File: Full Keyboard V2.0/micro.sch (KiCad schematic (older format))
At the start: 10 parts, among them J1 Conn_01x26, U1 AT24C02, U3 CD74HC4067SM

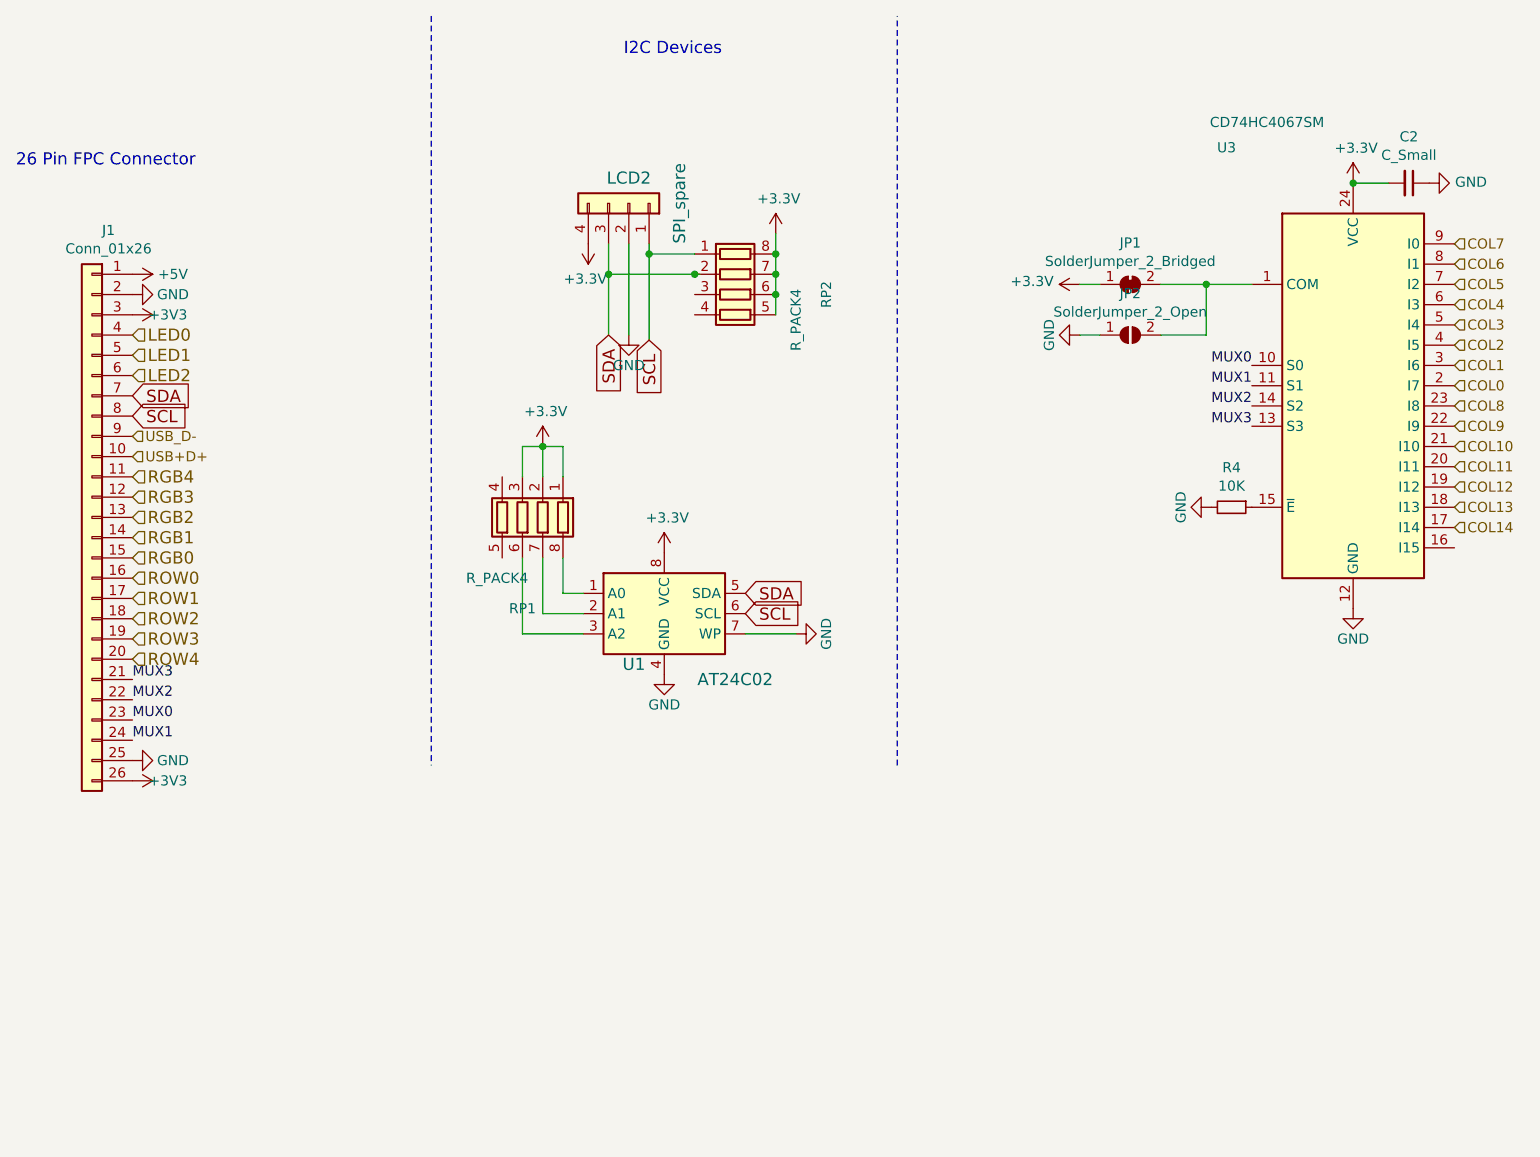
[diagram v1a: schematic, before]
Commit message: Added solder jumpers to allow for daisy chaining RGB rows
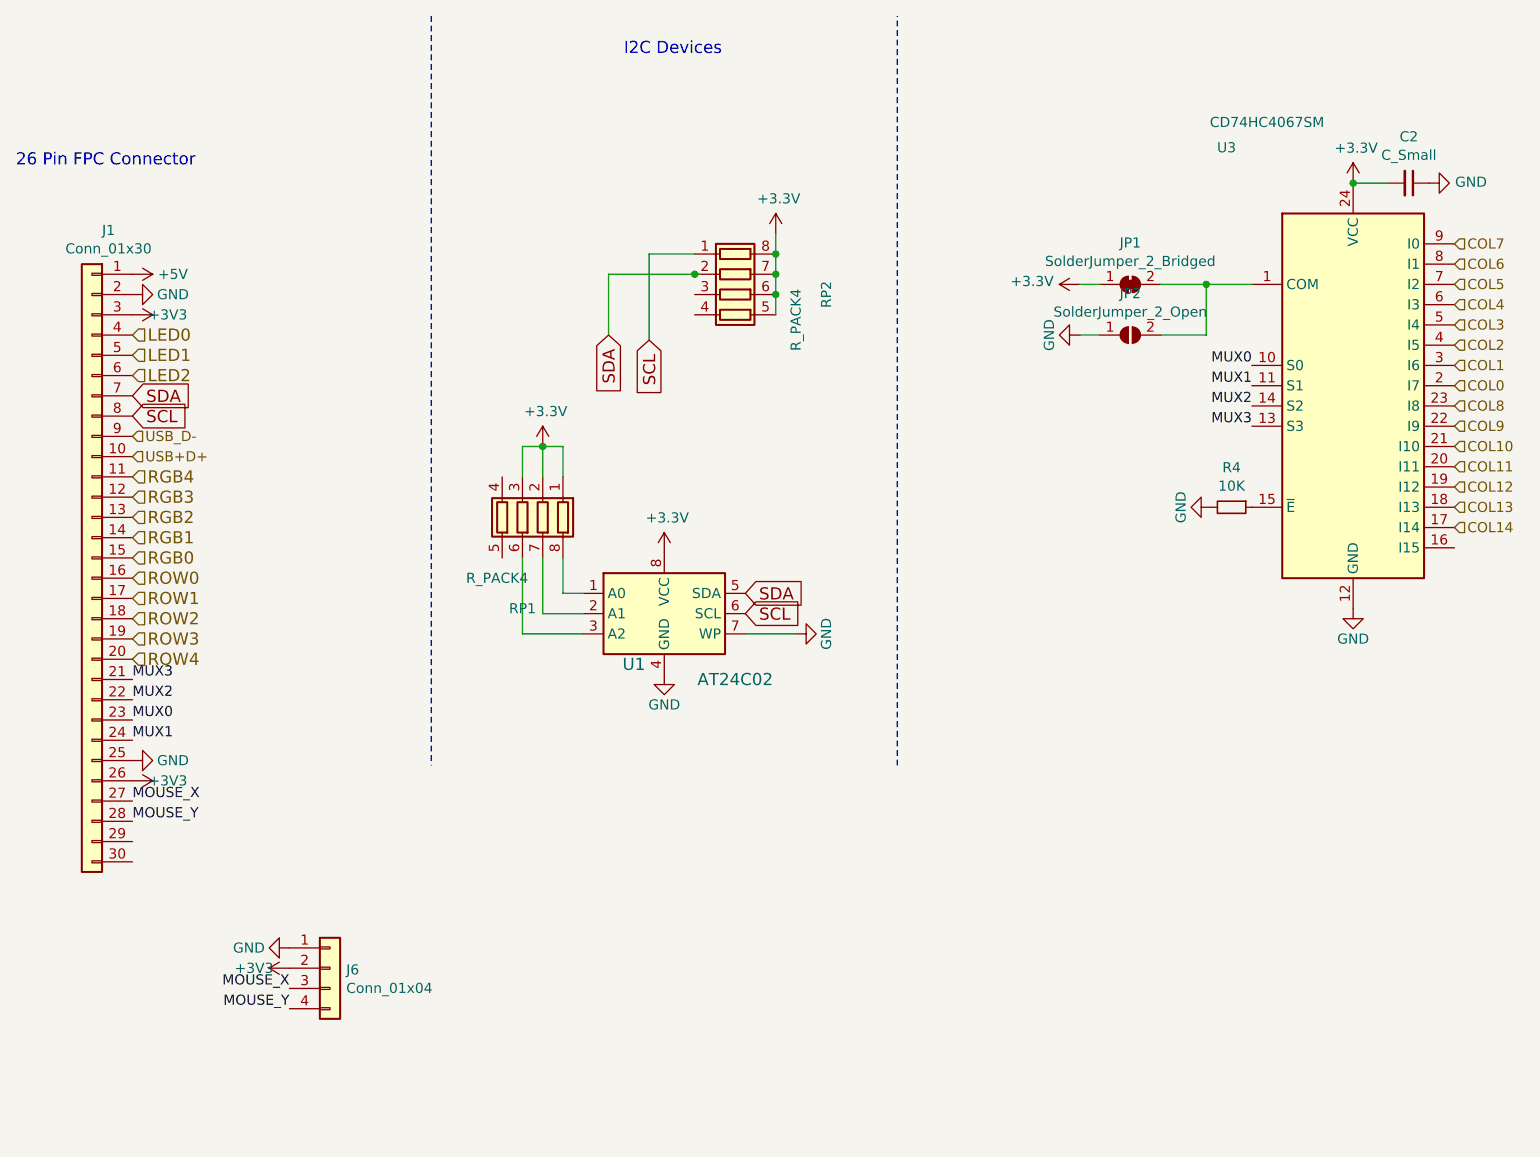
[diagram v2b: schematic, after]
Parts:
- removed J1: Conn_01x26, Connector_FFC-FPC:Hirose_FH12-26S-0.5SH_1x26-1MP_P0.50mm_Horizontal, symbol Connector_Generic:Conn_01x26
- removed LCD2: SPI_spare, Connector_PinHeader_2.54mm:PinHeader_1x04_P2.54mm_Vertical_SMD_Pin1Left, symbol Connector_Generic:Conn_01x04
- added J1: Conn_01x30, Connector_FFC-FPC:Hirose_FH12-30S-0.5SH_1x30-1MP_P0.50mm_Horizontal, symbol Connector_Generic:Conn_01x30
- added J6: Conn_01x04, Connector_JST:JST_PH_S4B-PH-SM4-TB_1x04-1MP_P2.00mm_Horizontal, symbol Connector_Generic:Conn_01x04
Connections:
- net labels added: MOUSE_X, MOUSE_Y
- wire segments 31 -> 28
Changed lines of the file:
@@
 $Descr A4 11693 8268
 encoding utf-8
-Sheet 3 4
+Sheet 2 4
 Title ""
 Date ""
@@
 	0    1    1    0
 $EndComp
-$Comp
-L Connector_Generic:Conn_01x04 LCD2
-U 1 1 59BADB3C
-P 5575 2775
-F 0 "LCD2" V 5700 2775 60  0000 C CNN
-F 1 "SPI_spare" H 5575 3025 60  0000 C CNN
-F 2 "Connector_PinHeader_2.54mm:PinHeader_1x04_P2.54mm_Vertical_SMD_Pin1Left" H 5575 2775 60  0001 C CNN
-F 3 "" H 5575 2775 60  0000 C CNN
-	1    5575 2775
-	0    1    -1   0
-$EndComp
 Text GLabel 5475 3425 3    60   Input ~ 0
 SDA
 Text GLabel 5675 3450 3    60   Input ~ 0
 SCL
-$Comp
-L power:GND #PWR0175
-U 1 1 59BADB44
-P 5575 3425
-F 0 "#PWR0175" H 5575 3175 50  0001 C CNN
-F 1 "GND" H 5575 3275 50  0000 C CNN
-F 2 "" H 5575 3425 50  0000 C CNN
-F 3 "" H 5575 3425 50  0000 C CNN
-	1    5575 3425
-	1    0    0    -1
-$EndComp
 Wire Wire Line
 	6400 4900 6150 4900
@@
 Wire Wire Line
 	5050 4900 5350 4900
-Wire Wire Line
-	5475 2975 5475 3125
 Wire Notes Line
 	6900 5550 6900 1850
@@
 Wire Wire Line
 	5900 3025 5675 3025
-Wire Wire Line
-	5675 2975 5675 3025
-Connection ~ 5675 3025
 Wire Wire Line
 	5675 3025 5675 3450
@@
 ROW0
 $Comp
-L Connector_Generic:Conn_01x26 J1
-U 1 1 5EAC1DE2
-P 2925 4325
-F 0 "J1" H 2843 5742 50  0000 C CNN
-F 1 "Conn_01x26" H 2843 5651 50  0000 C CNN
-F 2 "Connector_FFC-FPC:Hirose_FH12-26S-0.5SH_1x26-1MP_P0.50mm_Horizontal" H 2925 4325 50  0001 C CNN
-F 3 "~" H 2925 4325 50  0001 C CNN
-	1    2925 4325
-	-1   0    0    -1
-$EndComp
-$Comp
 L FullKeyboardV1-cache:+3.3V #PWR0168
 U 1 1 616DAE3A
@@
 $EndComp
 $Comp
-L FullKeyboardV1-cache:+3.3V #PWR0174
-U 1 1 616E0DE4
-P 5375 2975
-F 0 "#PWR0174" H 5375 2825 50  0001 C CNN
-F 1 "+3.3V" H 5390 3148 50  0000 C CNN
-F 2 "" H 5375 2975 50  0001 C CNN
-F 3 "" H 5375 2975 50  0001 C CNN
-	1    5375 2975
-	-1   0    0    1
-$EndComp
-$Comp
 L power:+3V3 #PWR0176
 U 1 1 616E35FA
@@
 $EndComp
 Wire Wire Line
-	5575 2975 5575 3425
-Wire Wire Line
 	5925 3125 5900 3125
 Connection ~ 5900 3125
@@
 Wire Wire Line
 	5475 3425 5475 3125
-Connection ~ 5475 3125
 $Comp
 L Device:R_Pack04 RP1
@@
 	0    1    1    0
 $EndComp
+$Comp
+L Connector_Generic:Conn_01x30 J1
+U 1 1 5E9DC884
+P 2925 4525
+F 0 "J1" H 2843 6142 50  0000 C CNN
+F 1 "Conn_01x30" H 2843 6051 50  0000 C CNN
+F 2 "Connector_FFC-FPC:Hirose_FH12-30S-0.5SH_1x30-1MP_P0.50mm_Horizontal" H 2925 4525 50  0001 C CNN
+F 3 "~" H 2925 4525 50  0001 C CNN
+	1    2925 4525
+	-1   0    0    -1
+$EndComp
+$Comp
+L Connector_Generic:Conn_01x04 J6
+U 1 1 5E9E6B8A
+P 4100 6550
+F 0 "J6" H 4180 6542 50  0000 L CNN
+F 1 "Conn_01x04" H 4180 6451 50  0000 L CNN
+F 2 "Connector_JST:JST_PH_S4B-PH-SM4-TB_1x04-1MP_P2.00mm_Horizontal" H 4100 6550 50  0001 C CNN
+F 3 "~" H 4100 6550 50  0001 C CNN
+	1    4100 6550
+	1    0    0    -1
+$EndComp
+Text Label 3900 6650 2    50   ~ 0
+MOUSE_X
+Text Label 3900 6750 2    50   ~ 0
+MOUSE_Y
+$Comp
+L power:+3V3 #PWR0166
+U 1 1 5E9E9956
+P 3900 6550
+F 0 "#PWR0166" H 3900 6400 50  0001 C CNN
+F 1 "+3V3" V 3900 6725 50  0000 C CNN
+F 2 "" H 3900 6550 50  0000 C CNN
+F 3 "" H 3900 6550 50  0000 C CNN
+	1    3900 6550
+	0    -1   -1   0
+$EndComp
+$Comp
+L power:GND #PWR0222
+U 1 1 5E9E9F7B
+P 3900 6450
+F 0 "#PWR0222" H 3900 6200 50  0001 C CNN
+F 1 "GND" V 3900 6250 50  0000 C CNN
+F 2 "" H 3900 6450 50  0000 C CNN
+F 3 "" H 3900 6450 50  0000 C CNN
+	1    3900 6450
+	0    1    1    0
+$EndComp
+Text Label 3125 5725 0    50   ~ 0
+MOUSE_X
+Text Label 3125 5825 0    50   ~ 0
+MOUSE_Y
 $EndSCHEMATC

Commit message: Added BOOT switch
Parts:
- added SW14: SW_SPDT, keyboard:SS12F23, symbol Switch:SW_SPDT
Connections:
- net labels added: BOOT_SWITCH
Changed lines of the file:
@@
 	6900 5550 6900 1850
 Wire Notes Line
-	4600 1850 4600 5550
+	4125 3125 4125 6825
 Text Notes 5550 2050 0    60   ~ 0
 I2C Devices
@@
 Text Label 3125 5825 0    50   ~ 0
 MOUSE_Y
+$Comp
+L Switch:SW_SPDT SW14
+U 1 1 5EA800B2
+P 4025 7250
+F 0 "SW14" H 4025 7535 50  0000 C CNN
+F 1 "SW_SPDT" H 4025 7444 50  0000 C CNN
+F 2 "keyboard:SS12F23" H 4025 7250 50  0001 C CNN
+F 3 "~" H 4025 7250 50  0001 C CNN
+	1    4025 7250
+	1    0    0    -1
+$EndComp
+Text Label 3125 5925 0    50   ~ 0
+BOOT_SWITCH
+Text Label 3825 7250 2    50   ~ 0
+BOOT_SWITCH
+$Comp
+L power:+3V3 #PWR0174
+U 1 1 5EA8BEDB
+P 4225 7150
+F 0 "#PWR0174" H 4225 7000 50  0001 C CNN
+F 1 "+3V3" V 4225 7325 50  0000 C CNN
+F 2 "" H 4225 7150 50  0000 C CNN
+F 3 "" H 4225 7150 50  0000 C CNN
+	1    4225 7150
+	0    1    1    0
+$EndComp
+$Comp
+L power:GND #PWR0175
+U 1 1 5EA8C396
+P 4225 7350
+F 0 "#PWR0175" H 4225 7100 50  0001 C CNN
+F 1 "GND" V 4225 7150 50  0000 C CNN
+F 2 "" H 4225 7350 50  0000 C CNN
+F 3 "" H 4225 7350 50  0000 C CNN
+	1    4225 7350
+	0    -1   -1   0
+$EndComp
 $EndSCHEMATC
